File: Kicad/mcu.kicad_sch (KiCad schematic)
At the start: 19 parts, among them J10 Conn_01x03_Pin, J2 USB_B_Micro, J4 Conn_02x03_Top_Bottom, U4 STM32G431CBT6

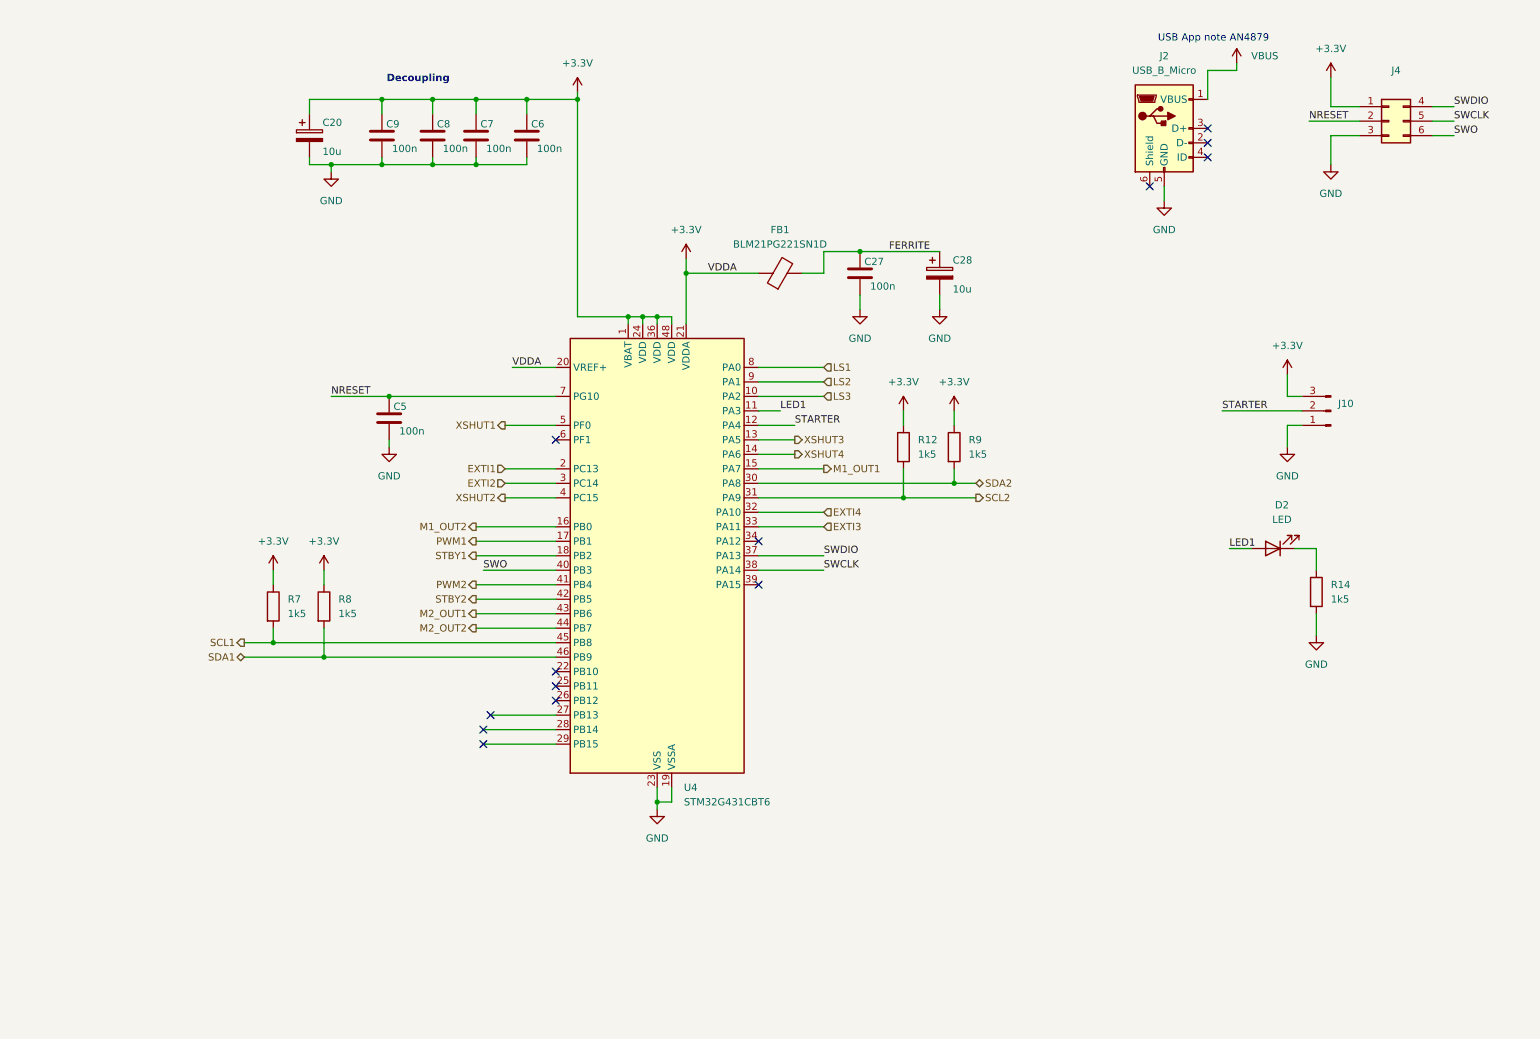
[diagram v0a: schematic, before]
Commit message: finished pcb - added pwm resistors, and fixed VDDA decoupling
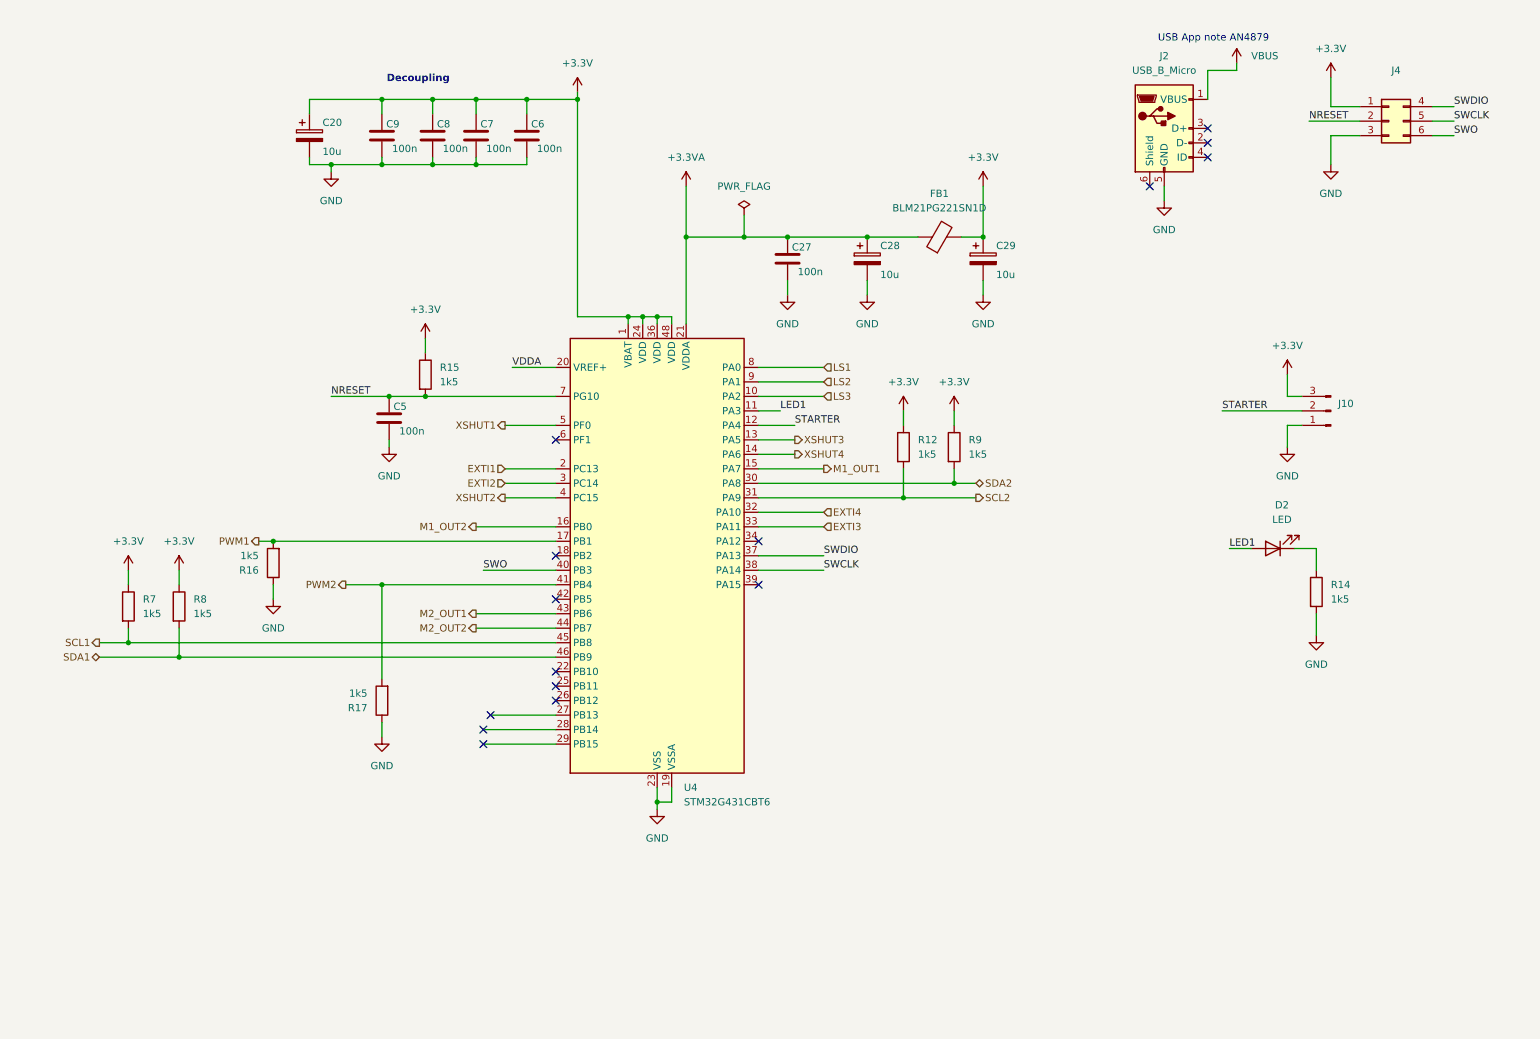
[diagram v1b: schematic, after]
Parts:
- added C29: 10u, Capacitor_Tantalum_SMD:CP_EIA-3528-12_Kemet-T_HandSolder, symbol Device:C_Polarized
- added R15, R16, R17: 1k5, Resistor_SMD:R_0805_2012Metric_Pad1.20x1.40mm_HandSolder, symbol Device:R
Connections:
- net +3.3V: now also FB1.2, C29.1, R15.1; no longer FB1.1, U4.20 (VREF+), U4.21 (VDDA)
- net GND: now also C29.2, R16.1, R17.1
- net NRESET: now also R15.2
- net PWM1: now also R16.2
- net PWM2: now also R17.2
- net FERRITE renamed +3.3VA
- net +3.3VA: now also FB1.1, U4.21 (VDDA); no longer FB1.2
- net STBY1: no longer names the net of U4.18 (PB2)
- net STBY2: no longer names the net of U4.42 (PB5)
- new net VDDA: U4.20 (VREF+)
- no-connect marks 13 -> 15
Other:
- moved on the sheet: C27, C28, FB1, R7, R8

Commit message: not small changes
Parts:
- J10: footprint Connector_PinSocket_2.54mm:PinSocket_1x03_P2.54mm_Vertical -> Connector_PinHeader_2.54mm:PinHeader_1x03_P2.54mm_Vertical
- J4: footprint Connector_PinSocket_2.54mm:PinSocket_2x03_P2.54mm_Vertical -> Connector_PinHeader_2.54mm:PinHeader_2x03_P2.54mm_Vertical
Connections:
- net +3.3V: now also J4.2 (Pin_2); no longer J4.1 (Pin_1)
- net GND: now also J4.4 (Pin_4); no longer J4.3 (Pin_3)
- net NRESET: now also J4.1 (Pin_1); no longer J4.2 (Pin_2)
- net SWCLK: now also J4.6 (Pin_6); no longer J4.5 (Pin_5)
- net SWDIO: now also J4.3 (Pin_3); no longer J4.4 (Pin_4)
- net SWO: now also J4.5 (Pin_5); no longer J4.6 (Pin_6)
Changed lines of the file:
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@@
 	(wire
 		(pts
-			(xy 35.56 124.46) (xy 35.56 127)
-		)
-		(stroke
-			(width 0)
-			(type default)
-		)
-	)
-	(wire
-		(pts
-			(xy 171.45 96.52) (xy 171.45 101.6)
+			(xy 264.16 33.02) (xy 264.16 26.67)
 		)
 		(stroke
@@
 	(wire
 		(pts
-			(xy 81.28 91.44) (xy 81.28 92.71)
+			(xy 35.56 124.46) (xy 35.56 127)
 		)
 		(stroke
@@
 	(wire
 		(pts
-			(xy 264.16 38.1) (xy 267.97 38.1)
+			(xy 171.45 96.52) (xy 171.45 101.6)
 		)
 		(stroke
@@
 	(wire
 		(pts
-			(xy 251.46 38.1) (xy 246.38 38.1)
+			(xy 81.28 91.44) (xy 81.28 92.71)
 		)
 		(stroke
@@
 	(wire
 		(pts
+			(xy 248.92 38.1) (xy 251.46 38.1)
+		)
+		(stroke
+			(width 0)
+			(type default)
+		)
+	)
+	(wire
+		(pts
+			(xy 243.84 33.02) (xy 251.46 33.02)
+		)
+		(stroke
+			(width 0)
+			(type default)
+		)
+	)
+	(wire
+		(pts
 			(xy 227.33 86.36) (xy 241.3 86.36)
 		)
@@
 	(wire
 		(pts
+			(xy 241.3 27.94) (xy 241.3 35.56)
+		)
+		(stroke
+			(width 0)
+			(type default)
+		)
+	)
+	(wire
+		(pts
 			(xy 114.3 31.75) (xy 114.3 69.85)
 		)
@@
 	(wire
 		(pts
-			(xy 264.16 33.02) (xy 267.97 33.02)
+			(xy 128.27 69.85) (xy 128.27 71.12)
 		)
 		(stroke
@@
 	(wire
 		(pts
-			(xy 128.27 69.85) (xy 128.27 71.12)
+			(xy 264.16 26.67) (xy 271.78 26.67)
 		)
 		(stroke
@@
 	(wire
 		(pts
-			(xy 185.42 63.5) (xy 185.42 66.04)
+			(xy 241.3 35.56) (xy 251.46 35.56)
 		)
 		(stroke
@@
 	(wire
 		(pts
-			(xy 128.27 152.4) (xy 128.27 154.94)
+			(xy 185.42 63.5) (xy 185.42 66.04)
 		)
 		(stroke
@@
 	(wire
 		(pts
-			(xy 80.01 116.84) (xy 80.01 133.35)
+			(xy 128.27 152.4) (xy 128.27 154.94)
 		)
 		(stroke
@@
 	(wire
 		(pts
-			(xy 146.05 104.14) (xy 157.48 104.14)
+			(xy 80.01 116.84) (xy 80.01 133.35)
 		)
 		(stroke
@@
 	(wire
 		(pts
-			(xy 97.79 114.3) (xy 110.49 114.3)
+			(xy 146.05 104.14) (xy 157.48 104.14)
 		)
 		(stroke
@@
 	(wire
 		(pts
-			(xy 229.87 26.67) (xy 229.87 25.4)
+			(xy 97.79 114.3) (xy 110.49 114.3)
 		)
 		(stroke
@@
 	(wire
 		(pts
-			(xy 246.38 38.1) (xy 246.38 43.18)
+			(xy 229.87 26.67) (xy 229.87 25.4)
 		)
 		(stroke
@@
 	(wire
 		(pts
-			(xy 246.38 33.02) (xy 246.38 27.94)
-		)
-		(stroke
-			(width 0)
-			(type default)
-		)
-	)
-	(wire
-		(pts
 			(xy 35.56 114.3) (xy 35.56 116.84)
 		)
@@
 	(wire
 		(pts
-			(xy 242.57 35.56) (xy 251.46 35.56)
-		)
-		(stroke
-			(width 0)
-			(type default)
-		)
-	)
-	(wire
-		(pts
 			(xy 96.52 106.68) (xy 110.49 106.68)
 		)
@@
 	(wire
 		(pts
-			(xy 246.38 33.02) (xy 251.46 33.02)
-		)
-		(stroke
-			(width 0)
-			(type default)
-		)
-	)
-	(wire
-		(pts
 			(xy 80.01 31.75) (xy 80.01 34.29)
 		)
@@
 	(wire
 		(pts
-			(xy 264.16 35.56) (xy 267.97 35.56)
+			(xy 264.16 38.1) (xy 267.97 38.1)
 		)
 		(stroke
@@
 	(wire
 		(pts
+			(xy 264.16 35.56) (xy 267.97 35.56)
+		)
+		(stroke
+			(width 0)
+			(type default)
+		)
+	)
+	(wire
+		(pts
 			(xy 125.73 69.85) (xy 125.73 71.12)
 		)
@@
 		)
 	)
+	(label "NRESET"
+		(at 243.84 33.02 0)
+		(effects
+			(font
+				(size 1.27 1.27)
+			)
+			(justify left bottom)
+		)
+	)
 	(label "VDDA"
 		(at 102.87 78.74 0)
@@
 	)
 	(label "SWDIO"
-		(at 267.97 33.02 0)
+		(at 248.92 38.1 180)
 		(effects
 			(font
 				(size 1.27 1.27)
 			)
-			(justify left bottom)
+			(justify right bottom)
 		)
 	)
@@
 	)
 	(label "SWCLK"
-		(at 267.97 35.56 0)
+		(at 267.97 38.1 0)
 		(effects
 			(font
@@
 		)
 	)
-	(label "NRESET"
-		(at 242.57 35.56 0)
-		(effects
-			(font
-				(size 1.27 1.27)
-			)
-			(justify left bottom)
-		)
-	)
 	(label "SWO"
 		(at 97.79 114.3 0)
@@
 	)
 	(label "SWO"
-		(at 267.97 38.1 0)
+		(at 267.97 35.56 0)
 		(effects
 			(font
@@
 	(symbol
 		(lib_id "power:GND")
-		(at 246.38 43.18 0)
+		(at 271.78 26.67 0)
 		(unit 1)
 		(exclude_from_sim no)
@@
 		(fields_autoplaced yes)
 		(property "Reference" "#PWR042"
-			(at 246.38 49.53 0)
+			(at 271.78 33.02 0)
 			(effects
 				(font
@@
 		)
 		(property "Value" "GND"
-			(at 246.38 48.26 0)
+			(at 271.78 31.75 0)
 			(effects
 				(font
@@
 		)
 		(property "Footprint" ""
-			(at 246.38 43.18 0)
+			(at 271.78 26.67 0)
 			(effects
 				(font
@@
 		)
 		(property "Datasheet" ""
-			(at 246.38 43.18 0)
+			(at 271.78 26.67 0)
 			(effects
 				(font
@@
 		)
 		(property "Description" "Power symbol creates a global label with name \"GND\" , ground"
-			(at 246.38 43.18 0)
+			(at 271.78 26.67 0)
 			(effects
 				(font
@@
 			)
 		)
-		(property "Footprint" "Connector_PinSocket_2.54mm:PinSocket_2x03_P2.54mm_Vertical"
+		(property "Footprint" "Connector_PinHeader_2.54mm:PinHeader_2x03_P2.54mm_Vertical"
 			(at 256.54 35.56 0)
 			(effects
@@
 			)
 		)
-		(property "Footprint" "Connector_PinSocket_2.54mm:PinSocket_1x03_P2.54mm_Vertical"
+		(property "Footprint" "Connector_PinHeader_2.54mm:PinHeader_1x03_P2.54mm_Vertical"
 			(at 246.38 86.36 0)
 			(effects
@@
 	(symbol
 		(lib_id "power:+3.3V")
-		(at 246.38 27.94 0)
+		(at 241.3 27.94 0)
 		(unit 1)
 		(exclude_from_sim no)
@@
 		(fields_autoplaced yes)
 		(property "Reference" "#PWR041"
-			(at 246.38 31.75 0)
+			(at 241.3 31.75 0)
 			(effects
 				(font
@@
 		)
 		(property "Value" "+3.3V"
-			(at 246.38 22.86 0)
+			(at 241.3 22.86 0)
 			(effects
 				(font
@@
 		)
 		(property "Footprint" ""
-			(at 246.38 27.94 0)
+			(at 241.3 27.94 0)
 			(effects
 				(font
@@
 		)
 		(property "Datasheet" ""
-			(at 246.38 27.94 0)
+			(at 241.3 27.94 0)
 			(effects
 				(font
@@
 		)
 		(property "Description" "Power symbol creates a global label with name \"+3.3V\""
-			(at 246.38 27.94 0)
+			(at 241.3 27.94 0)
 			(effects
 				(font

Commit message: fixed scheme with i2c
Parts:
- added R18: 1k5, Resistor_SMD:R_0805_2012Metric_Pad1.20x1.40mm_HandSolder, symbol Device:R
- R7: value 1k5 -> 10k
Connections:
- net +3.3V: now also R18.1; no longer R7.1
- net GND: now also R7.1
- net SCL1: now also U4.39 (PA15), R18.2; no longer R7.2, U4.45 (PB8)
- net SWO: no longer names the net of J4.5 (Pin_5)
- net SWO: no longer U4.40 (PB3)
- new net BOOT0: R7.2, U4.45 (PB8)
- no-connect marks 15 -> 16

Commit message: commit before - fixed start module, in kicad fix -- pcb with new scl1 route and boot0
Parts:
- removed R16: 1k5, Resistor_SMD:R_0805_2012Metric_Pad1.20x1.40mm_HandSolder, symbol Device:R
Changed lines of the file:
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@@
-	)
-	(junction
-		(at 60.96 109.22)
-		(diameter 0)
-		(color 0 0 0 0)
 	)
 	(junction
@@
 	(wire
 		(pts
-			(xy 58.42 109.22) (xy 60.96 109.22)
-		)
-		(stroke
-			(width 0)
-			(type default)
-		)
-	)
-	(wire
-		(pts
 			(xy 171.45 101.6) (xy 184.15 101.6)
 		)
@@
 	(wire
 		(pts
-			(xy 60.96 109.22) (xy 110.49 109.22)
+			(xy 58.42 109.22) (xy 110.49 109.22)
 		)
 		(stroke
@@
 		(pts
 			(xy 125.73 69.85) (xy 125.73 71.12)
-		)
-		(stroke
-			(width 0)
-			(type default)
-		)
-	)
-	(wire
-		(pts
-			(xy 60.96 119.38) (xy 60.96 116.84)
 		)
 		(stroke
@@
 	)
 	(symbol
-		(lib_id "Device:R")
-		(at 60.96 113.03 180)
-		(unit 1)
-		(exclude_from_sim no)
-		(in_bom yes)
-		(on_board yes)
-		(dnp no)
-		(fields_autoplaced yes)
-		(property "Reference" "R16"
-			(at 58.42 114.3001 0)
-			(effects
-				(font
-					(size 1.27 1.27)
-				)
-				(justify left)
-			)
-		)
-		(property "Value" "1k5"
-			(at 58.42 111.7601 0)
-			(effects
-				(font
-					(size 1.27 1.27)
-				)
-				(justify left)
-			)
-		)
-		(property "Footprint" "Resistor_SMD:R_0805_2012Metric_Pad1.20x1.40mm_HandSolder"
-			(at 62.738 113.03 90)
-			(effects
-				(font
-					(size 1.27 1.27)
-				)
-				(hide yes)
-			)
-		)
-		(property "Datasheet" "~"
-			(at 60.96 113.03 0)
-			(effects
-				(font
-					(size 1.27 1.27)
-				)
-				(hide yes)
-			)
-		)
-		(property "Description" "Resistor"
-			(at 60.96 113.03 0)
-			(effects
-				(font
-					(size 1.27 1.27)
-				)
-				(hide yes)
-			)
-		)
-		(pin "2"
-		)
-		(pin "1"
-		)
-		(instances
-			(project "MiniSumoSTM"
-				(path "/74ccf643-7ae0-4d9b-8b7c-e7e124cb3f26/49c74f4a-020b-47c6-ab92-88fca7232d7d"
-					(reference "R16")
-					(unit 1)
-				)
-			)
-		)
-	)
-	(symbol
 		(lib_id "power:GND")
 		(at 165.1 66.04 0)
@@
 					(unit 1)
 				)
-			)
-		)
-	)
-	(symbol
-		(lib_id "power:GND")
-		(at 60.96 119.38 0)
-		(unit 1)
-		(exclude_from_sim no)
-		(in_bom yes)
-		(on_board yes)
-		(dnp no)
-		(fields_autoplaced yes)
-		(property "Reference" "#PWR050"
-			(at 60.96 125.73 0)
-			(effects
-				(font
-					(size 1.27 1.27)
-				)
-				(hide yes)
-			)
-		)
-		(property "Value" "GND"
-			(at 60.96 124.46 0)
-			(effects
-				(font
-					(size 1.27 1.27)
-				)
-			)
-		)
-		(property "Footprint" ""
-			(at 60.96 119.38 0)
-			(effects
-				(font
-					(size 1.27 1.27)
-				)
-				(hide yes)
-			)
-		)
-		(property "Datasheet" ""
-			(at 60.96 119.38 0)
-			(effects
-				(font
-					(size 1.27 1.27)
-				)
-				(hide yes)
-			)
-		)
-		(property "Description" "Power symbol creates a global label with name \"GND\" , ground"
-			(at 60.96 119.38 0)
-			(effects
-				(font
-					(size 1.27 1.27)
-				)
-				(hide yes)
-			)
-		)
-		(pin "1"
-		)
-		(instances
-			(project "MiniSumoSTM"
-				(path "/74ccf643-7ae0-4d9b-8b7c-e7e124cb3f26/49c74f4a-020b-47c6-ab92-88fca7232d7d"
-					(reference "#PWR050")
-					(unit 1)
-				)
